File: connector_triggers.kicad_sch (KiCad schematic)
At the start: 6 parts, among them J2 JST_SH_1x6_SM06B-SRSS-TB-LF-SN, U10 TPD4E02B04DQA

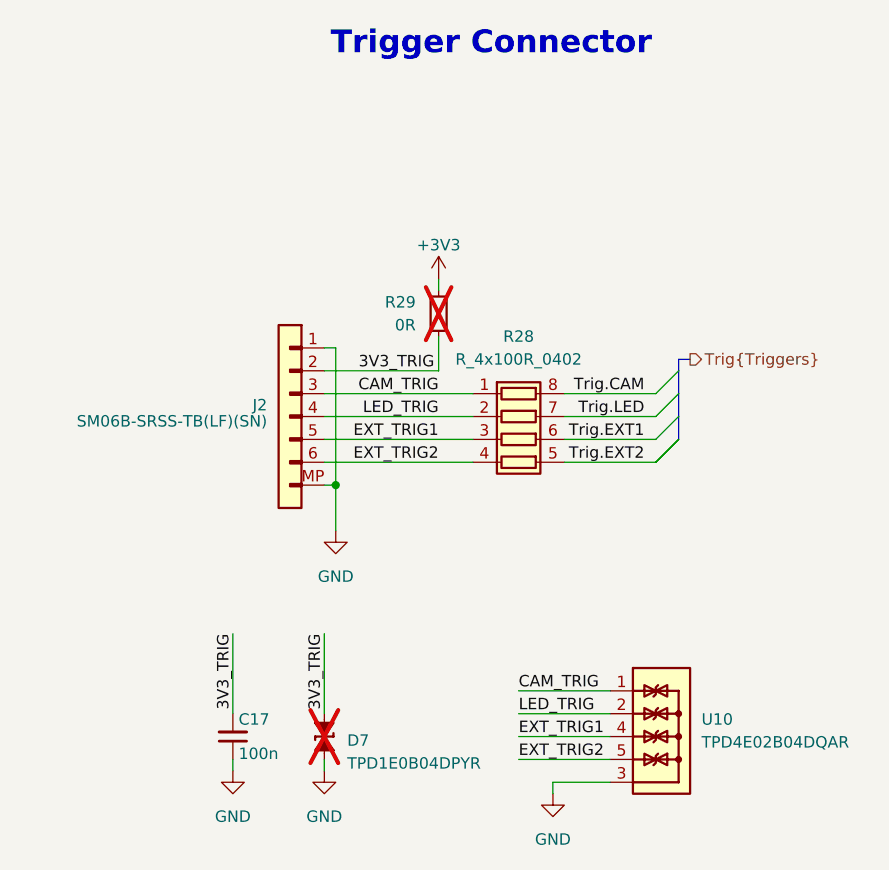
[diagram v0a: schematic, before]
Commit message: Bump to KiCad 9.x
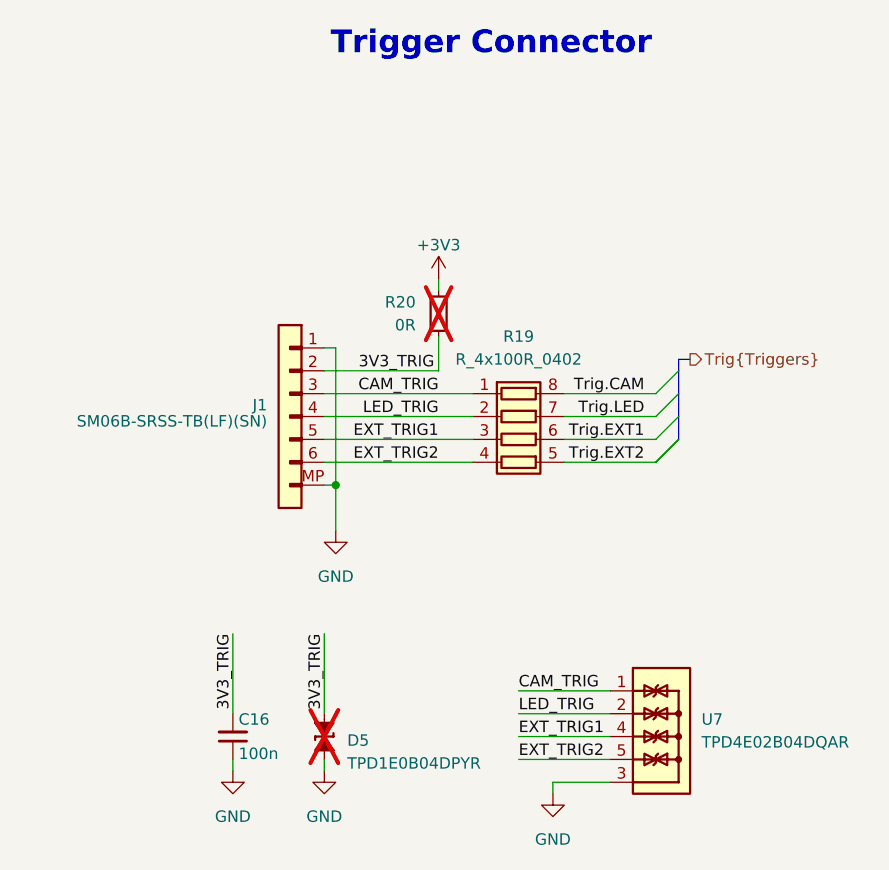
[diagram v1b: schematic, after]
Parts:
- renumbered C17 to C16, D7 to D5, J2 to J1, R28 to R19, R29 to R20, U10 to U7
